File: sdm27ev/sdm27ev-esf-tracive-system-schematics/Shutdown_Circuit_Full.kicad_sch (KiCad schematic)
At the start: 44 parts, among them J1 Precharge/Relay_Controller, K1 PR22-12V-400-1A, K2 PR22-12V-400-1A, K3 PR22-12V-400-1A, K4 Main Contactor Relay, K5 Isolation_Relay_+, K6 Isolation Relay -, K7 Precharge Relay, K8 Discharge Relay, Q1 ZXM61N02FTC, Q2 ZXM61N02FTC, Q3 ZXM61N02FTC, SW1 GLVMS, SW2 Inertia_Switch, SW3 Cockpit_Shutdown_Button, SW4 Right_Shutdown_Button, SW5 Left_Shutdown_Button, SW6 BOTS, SW7 TSMS, SW8 TS_Container_Interlock

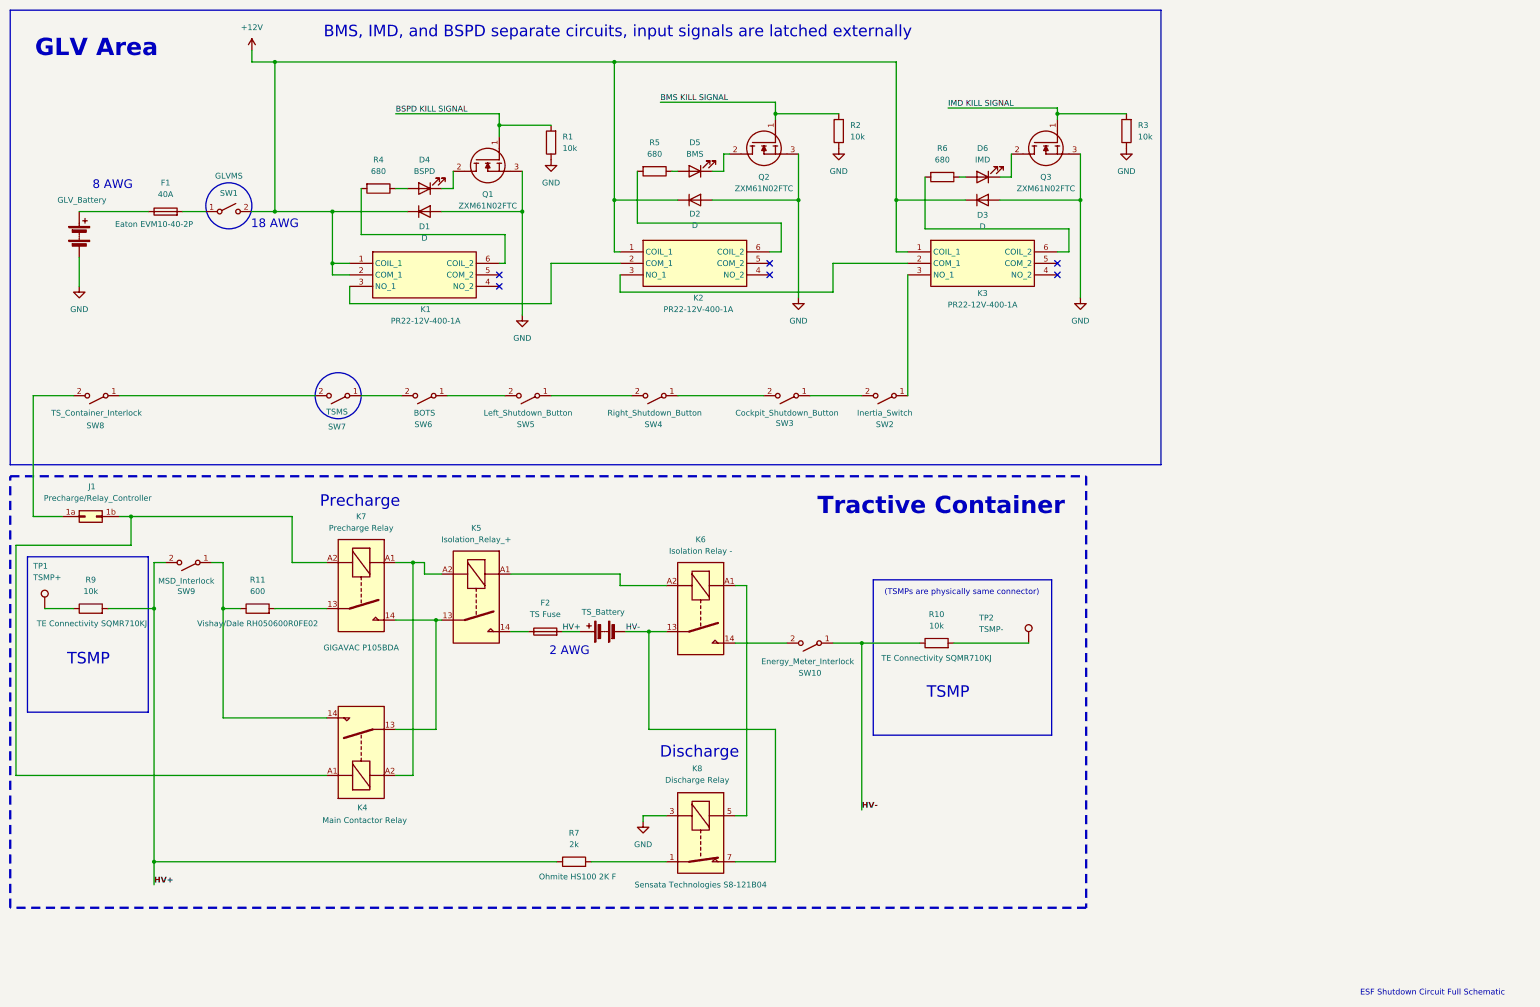
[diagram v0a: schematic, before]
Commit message: Updated Shutdown Circuit ESF Schematic
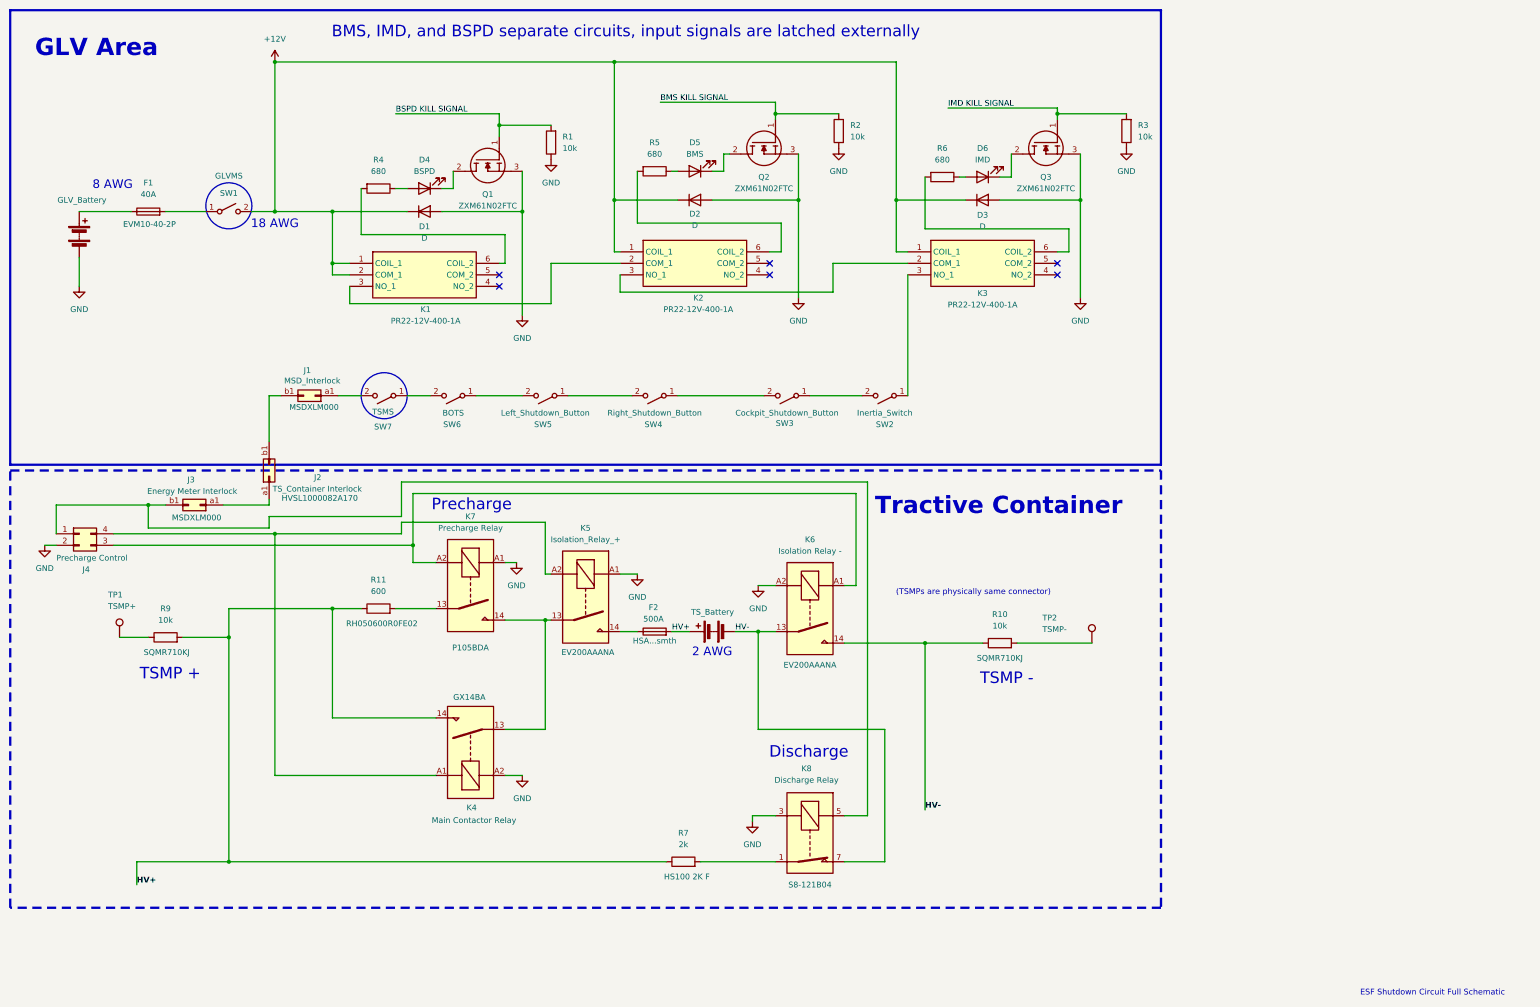
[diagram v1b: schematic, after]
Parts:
- removed Energy_Meter_Interlock: SW10, symbol Switch:SW_SPST
- removed J1: Precharge/Relay_Controller, symbol Connector_Generic:Conn_02x01_Row_Letter_Last
- removed MSD_Interlock: SW9, symbol Switch:SW_SPST
- removed SW8: TS_Container_Interlock, symbol Switch:SW_SPST
- added J1: MSD_Interlock, symbol Connector_Generic:Conn_02x01_Row_Letter_First
- added J2: TS_Container Interlock, symbol Connector_Generic:Conn_02x01_Row_Letter_First
- added J3: Energy Meter Interlock, symbol Connector_Generic:Conn_02x01_Row_Letter_First
- added J4: Precharge Control, symbol Connector_Generic:Conn_02x02_Counter_Clockwise
- F2: value TS Fuse -> 500A
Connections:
- net GND: now also K4.A2, K5.A1, K6.A2, K7.A1, J4.2 (Pin_2)
- net HV+: now also K4.14, R11.1
- net HV-: now also K6.14
- net at K6.A1: now also K7.A2, J4.3 (Pin_3); no longer K8.5
- net at K4.A1: now also K5.A2, J4.4 (Pin_4); no longer K7.A2
- net at SW7.2 (B): now also J1.a1 (Pin_a1)
- new net: J2.a1 (Pin_a1), J3.a1 (Pin_a1)
- new net: J1.b1 (Pin_b1), J2.b1 (Pin_b1)
- new net: J3.b1 (Pin_b1), J4.1 (Pin_1), K8.5
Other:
- note added: "TSMP +"
- note added: "TSMP -"
- note removed: "TSMP"
- moved on the sheet: F1, F2, K4, K5, K6, K7, K8, R10, R11, R7, R9, SW5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
